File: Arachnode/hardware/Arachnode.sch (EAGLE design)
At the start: 35 parts, among them J1 PINHEAD-17-REV, J2 PINHEAD-17-REV, U1 BQ24210, U2 DS1337

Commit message: ﻿-- added power switching to make USB power work correctly. # Please enter the commit message for your changes. Lines starting # with '#' will be ignored, and an empty message aborts the commit. # On branch arachnode-update # Your branch is up-to-date with 'origin/arachnode-update'. # # Changes to be committed: #	modified:   Arachnode/hardware/Arachnode.brd #	modified:   Arachnode/hardware/Arachnode.sch #
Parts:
- added R15: 4k7, resistor:R-EU_R0603
- added T1: (no value), zetex:PMOSSOT23
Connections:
- new net 3V3: J2.16, J2.33, JP2.16, T1.D
- net +5V: now also R15.2
- net N$1: now also R15.1, T1.G; no longer C1.2, R1.2, SOLAR.1A, SOLAR.1B, U1.VIN
- net VIN: now also C1.2, R1.2, SOLAR.1A, SOLAR.1B, U1.VIN
- net V_BATT: now also T1.S; no longer J2.16, J2.33, JP2.16
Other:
- moved on the sheet: SD
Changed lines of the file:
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@@
 <part name="C4" library="resistor" deviceset="C-EU" device="C0603" value="100n"/>
 <part name="GND14" library="supply1" deviceset="GND" device=""/>
+<part name="T1" library="zetex" deviceset="PMOSSOT23" device=""/>
+<part name="R15" library="resistor" deviceset="R-EU_" device="R0603" value="4k7"/>
 </parts>
 <sheets>
@@
 <instance part="GND1" gate="1" x="48.26" y="114.3"/>
 <instance part="GND2" gate="1" x="167.64" y="114.3"/>
-<instance part="SD" gate="G$1" x="231.14" y="144.78">
-<attribute name="PARTNO" x="231.14" y="144.78" size="1.778" layer="96" display="off"/>
-</instance>
-<instance part="GND3" gate="1" x="218.44" y="116.84"/>
-<instance part="SUPPLY4" gate="G$1" x="170.18" y="172.72"/>
-<instance part="SUPPLY6" gate="G$1" x="220.98" y="165.1"/>
+<instance part="SD" gate="G$1" x="53.34" y="68.58">
+<attribute name="PARTNO" x="53.34" y="68.58" size="1.778" layer="96" display="off"/>
+</instance>
+<instance part="GND3" gate="1" x="40.64" y="40.64"/>
+<instance part="SUPPLY4" gate="G$1" x="228.6" y="129.54"/>
+<instance part="SUPPLY6" gate="G$1" x="43.18" y="88.9"/>
 <instance part="J1" gate="G$1" x="68.58" y="142.24"/>
 <instance part="J2" gate="G$1" x="160.02" y="142.24" rot="MR0"/>
@@
 <instance part="C4" gate="G$1" x="93.98" y="104.14"/>
 <instance part="GND14" gate="1" x="93.98" y="93.98"/>
+<instance part="T1" gate="A" x="218.44" y="124.46" rot="MR270"/>
+<instance part="R15" gate="G$1" x="203.2" y="149.86" rot="R180"/>
 </instances>
 <busses>
@@
 <segment>
 <pinref part="SD" gate="G$1" pin="CS"/>
-<wire x1="223.52" y1="154.94" x2="208.28" y2="154.94" width="0.1524" layer="91"/>
-<label x="208.28" y="154.94" size="1.778" layer="95"/>
+<wire x1="45.72" y1="78.74" x2="30.48" y2="78.74" width="0.1524" layer="91"/>
+<label x="30.48" y="78.74" size="1.778" layer="95"/>
 </segment>
 </net>
@@
 <segment>
 <pinref part="SD" gate="G$1" pin="GND"/>
-<wire x1="223.52" y1="144.78" x2="218.44" y2="144.78" width="0.1524" layer="91"/>
-<wire x1="218.44" y1="144.78" x2="218.44" y2="134.62" width="0.1524" layer="91"/>
+<wire x1="45.72" y1="68.58" x2="40.64" y2="68.58" width="0.1524" layer="91"/>
+<wire x1="40.64" y1="68.58" x2="40.64" y2="58.42" width="0.1524" layer="91"/>
 <pinref part="SD" gate="G$1" pin="SHIELD@1"/>
-<wire x1="218.44" y1="134.62" x2="218.44" y2="132.08" width="0.1524" layer="91"/>
-<wire x1="218.44" y1="132.08" x2="218.44" y2="129.54" width="0.1524" layer="91"/>
-<wire x1="218.44" y1="129.54" x2="218.44" y2="127" width="0.1524" layer="91"/>
-<wire x1="218.44" y1="127" x2="218.44" y2="119.38" width="0.1524" layer="91"/>
-<wire x1="223.52" y1="134.62" x2="218.44" y2="134.62" width="0.1524" layer="91"/>
+<wire x1="40.64" y1="58.42" x2="40.64" y2="55.88" width="0.1524" layer="91"/>
+<wire x1="40.64" y1="55.88" x2="40.64" y2="53.34" width="0.1524" layer="91"/>
+<wire x1="40.64" y1="53.34" x2="40.64" y2="50.8" width="0.1524" layer="91"/>
+<wire x1="40.64" y1="50.8" x2="40.64" y2="43.18" width="0.1524" layer="91"/>
+<wire x1="45.72" y1="58.42" x2="40.64" y2="58.42" width="0.1524" layer="91"/>
 <pinref part="SD" gate="G$1" pin="SHIELD@2"/>
-<wire x1="223.52" y1="132.08" x2="218.44" y2="132.08" width="0.1524" layer="91"/>
+<wire x1="45.72" y1="55.88" x2="40.64" y2="55.88" width="0.1524" layer="91"/>
 <pinref part="SD" gate="G$1" pin="SHIELD@3"/>
-<wire x1="223.52" y1="129.54" x2="218.44" y2="129.54" width="0.1524" layer="91"/>
+<wire x1="45.72" y1="53.34" x2="40.64" y2="53.34" width="0.1524" layer="91"/>
 <pinref part="SD" gate="G$1" pin="SHIELD@4"/>
-<wire x1="223.52" y1="127" x2="218.44" y2="127" width="0.1524" layer="91"/>
+<wire x1="45.72" y1="50.8" x2="40.64" y2="50.8" width="0.1524" layer="91"/>
 <pinref part="GND3" gate="1" pin="GND"/>
-<junction x="218.44" y="127"/>
-<junction x="218.44" y="129.54"/>
-<junction x="218.44" y="132.08"/>
-<junction x="218.44" y="134.62"/>
+<junction x="40.64" y="50.8"/>
+<junction x="40.64" y="53.34"/>
+<junction x="40.64" y="55.88"/>
+<junction x="40.64" y="58.42"/>
 </segment>
 <segment>
@@
 <segment>
 <pinref part="SD" gate="G$1" pin="DO"/>
-<wire x1="223.52" y1="142.24" x2="208.28" y2="142.24" width="0.1524" layer="91"/>
-<label x="208.28" y="142.24" size="1.778" layer="95"/>
+<wire x1="45.72" y1="66.04" x2="30.48" y2="66.04" width="0.1524" layer="91"/>
+<label x="30.48" y="66.04" size="1.778" layer="95"/>
 </segment>
 </net>
@@
 <segment>
 <pinref part="SD" gate="G$1" pin="SCK"/>
-<wire x1="223.52" y1="147.32" x2="208.28" y2="147.32" width="0.1524" layer="91"/>
-<label x="208.28" y="147.32" size="1.778" layer="95"/>
+<wire x1="45.72" y1="71.12" x2="30.48" y2="71.12" width="0.1524" layer="91"/>
+<label x="30.48" y="71.12" size="1.778" layer="95"/>
 </segment>
 </net>
@@
 <segment>
 <pinref part="SD" gate="G$1" pin="DI"/>
-<wire x1="223.52" y1="152.4" x2="208.28" y2="152.4" width="0.1524" layer="91"/>
-<label x="208.28" y="152.4" size="1.778" layer="95"/>
+<wire x1="45.72" y1="76.2" x2="30.48" y2="76.2" width="0.1524" layer="91"/>
+<label x="30.48" y="76.2" size="1.778" layer="95"/>
 </segment>
 </net>
@@
 <junction x="162.56" y="149.86"/>
 <pinref part="JP2" gate="G$1" pin="6"/>
+<pinref part="R15" gate="G$1" pin="2"/>
+<wire x1="190.5" y1="149.86" x2="198.12" y2="149.86" width="0.1524" layer="91"/>
+<junction x="190.5" y="149.86"/>
 </segment>
 </net>
 <net name="V_BATT" class="0">
 <segment>
-<wire x1="190.5" y1="124.46" x2="170.18" y2="124.46" width="0.1524" layer="91"/>
-<label x="172.72" y="124.46" size="1.778" layer="95"/>
-<wire x1="170.18" y1="124.46" x2="162.56" y2="124.46" width="0.1524" layer="91"/>
-<wire x1="170.18" y1="124.46" x2="170.18" y2="172.72" width="0.1524" layer="91"/>
-<junction x="170.18" y="124.46"/>
-<pinref part="SUPPLY4" gate="G$1" pin="V_BATT"/>
-<pinref part="J2" gate="G$1" pin="16"/>
-<pinref part="J2" gate="G$1" pin="33"/>
-<junction x="162.56" y="124.46"/>
-<pinref part="JP2" gate="G$1" pin="16"/>
-</segment>
-<segment>
 <pinref part="SD" gate="G$1" pin="VCC"/>
-<wire x1="223.52" y1="149.86" x2="220.98" y2="149.86" width="0.1524" layer="91"/>
-<wire x1="220.98" y1="149.86" x2="220.98" y2="165.1" width="0.1524" layer="91"/>
+<wire x1="45.72" y1="73.66" x2="43.18" y2="73.66" width="0.1524" layer="91"/>
+<wire x1="43.18" y1="73.66" x2="43.18" y2="88.9" width="0.1524" layer="91"/>
 <pinref part="SUPPLY6" gate="G$1" pin="V_BATT"/>
 </segment>
@@
 <junction x="93.98" y="111.76"/>
 </segment>
+<segment>
+<pinref part="T1" gate="A" pin="S"/>
+<pinref part="SUPPLY4" gate="G$1" pin="V_BATT"/>
+<wire x1="223.52" y1="124.46" x2="228.6" y2="124.46" width="0.1524" layer="91"/>
+<wire x1="228.6" y1="124.46" x2="228.6" y2="129.54" width="0.1524" layer="91"/>
+</segment>
 </net>
 <net name="IO12" class="0">
@@
 <wire x1="88.9" y1="129.54" x2="139.7" y2="129.54" width="0.1524" layer="91"/>
 <wire x1="139.7" y1="129.54" x2="139.7" y2="147.32" width="0.1524" layer="91"/>
+</segment>
+</net>
+<net name="N$1" class="0">
+<segment>
+<pinref part="R15" gate="G$1" pin="1"/>
+<pinref part="T1" gate="A" pin="G"/>
+<wire x1="208.28" y1="149.86" x2="220.98" y2="149.86" width="0.1524" layer="91"/>
+<wire x1="220.98" y1="149.86" x2="220.98" y2="129.54" width="0.1524" layer="91"/>
+</segment>
+</net>
+<net name="3V3" class="0">
+<segment>
+<wire x1="190.5" y1="124.46" x2="162.56" y2="124.46" width="0.1524" layer="91"/>
+<label x="172.72" y="124.46" size="1.778" layer="95"/>
+<pinref part="J2" gate="G$1" pin="16"/>
+<pinref part="J2" gate="G$1" pin="33"/>
+<junction x="162.56" y="124.46"/>
+<pinref part="JP2" gate="G$1" pin="16"/>
+<junction x="190.5" y="124.46"/>
+<pinref part="T1" gate="A" pin="D"/>
+<wire x1="190.5" y1="124.46" x2="213.36" y2="124.46" width="0.1524" layer="91"/>
 </segment>
 </net>
@@
 </segment>
 </net>
-<net name="N$1" class="0">
+<net name="VIN" class="0">
 <segment>
 <wire x1="38.1" y1="124.46" x2="48.26" y2="124.46" width="0.1524" layer="91"/>
@@
 <wire x1="71.12" y1="114.3" x2="71.12" y2="124.46" width="0.1524" layer="91"/>
 <junction x="71.12" y="124.46"/>
-</segment>
-</net>
+<label x="58.42" y="124.46" size="1.778" layer="95"/>
+</segment>
+</net>

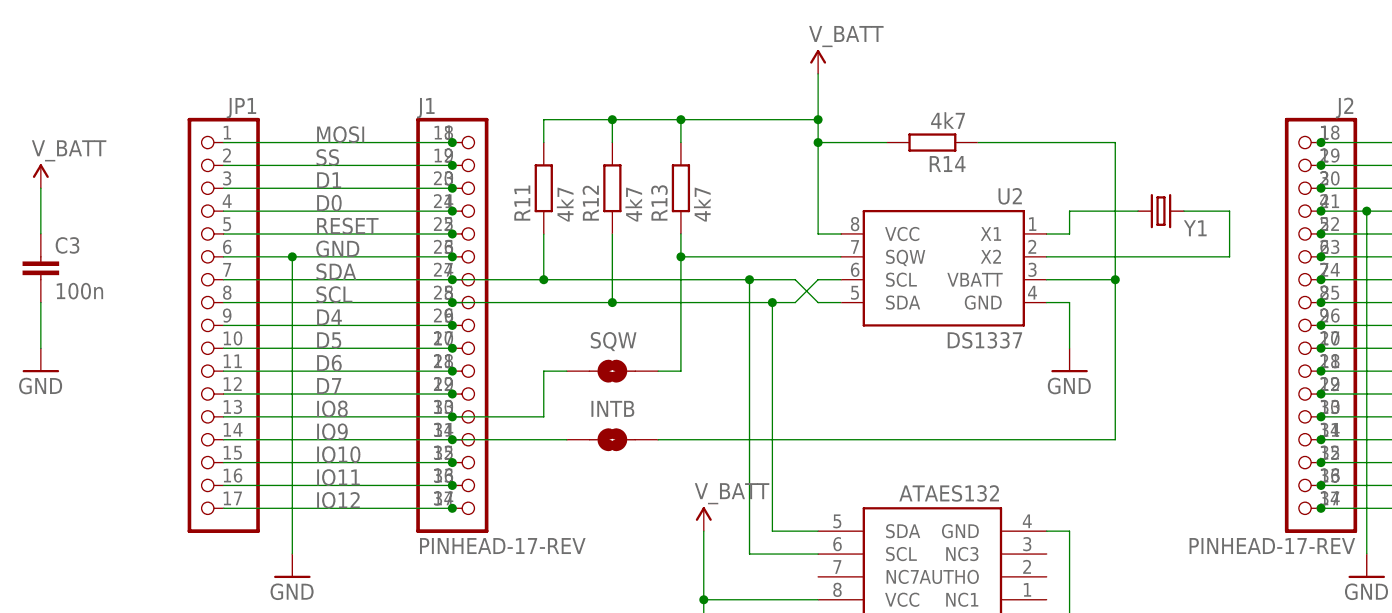
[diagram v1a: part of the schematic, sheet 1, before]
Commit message: Modified ArachnNode to Arachnio Due standard
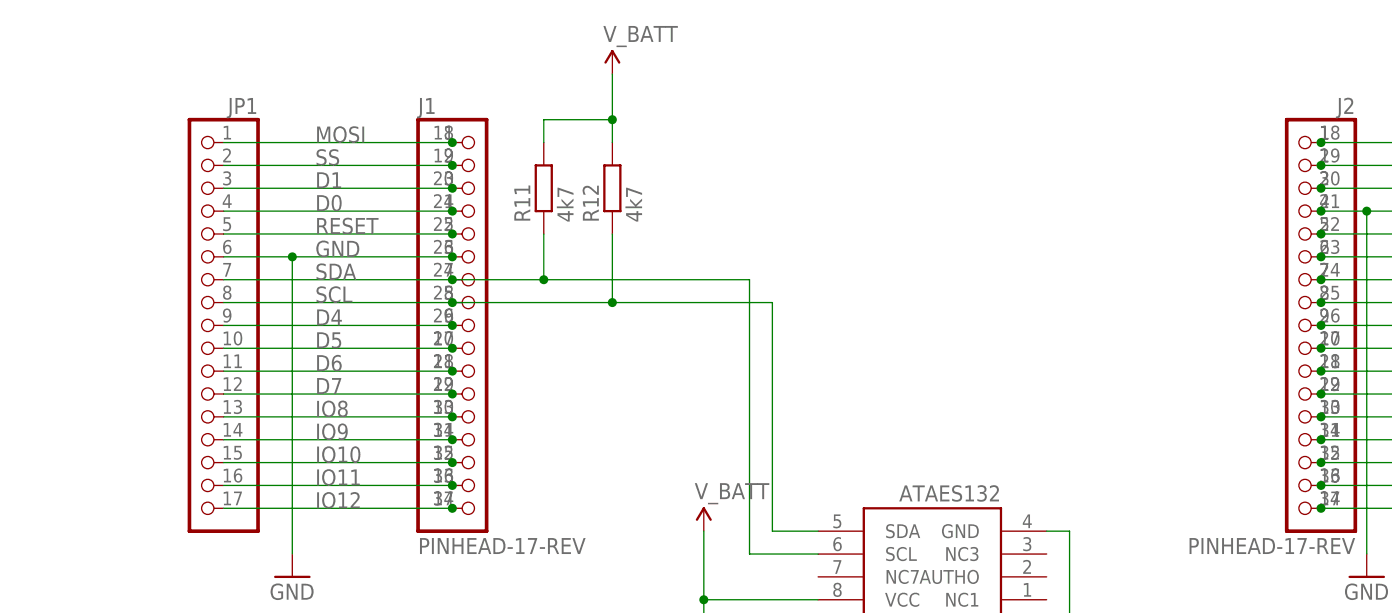
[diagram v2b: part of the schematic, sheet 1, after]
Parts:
- removed C3: 100n, resistor:C-EUC0603
- removed INTB, SQW: JUMPER-PAD-2-NOYES_SILK, SparkFun-Passives:JUMPER-PAD-2-NOYES_SILK
- removed R13, R14: 4k7, resistor:R-EU_R0603
- removed U2: DS1337, SparkFun-FreqCtrl:DS1307SO8-TIGHT
- removed Y1: (no value), SparkFun-FreqCtrl:CRYSTALEPSONMC146
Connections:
- removed net N$14: U2.X2, Y1.2
- removed net N$15: INTB.2, R14.1, U2.VBATT
- removed net N$2: R13.1, SQW.2, U2.SQW
- removed net N$4: U2.X1, Y1.1
- net GND: no longer C3.2, U2.GND
- net IO8: no longer SQW.1
- net IO9: no longer INTB.1
- net SCL: no longer U2.SCL
- net SDA: no longer U2.SDA
- net V_BATT: no longer C3.1, R13.2, R14.2, U2.VCC
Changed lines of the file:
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@@
 <part name="!CHG!" library="SparkFun-Passives" deviceset="JUMPER-PAD-2-NC_BY_TRACE" device=""/>
 <part name="!PG!" library="SparkFun-Passives" deviceset="JUMPER-PAD-2-NC_BY_TRACE" device=""/>
-<part name="U2" library="SparkFun-FreqCtrl" deviceset="DS1307" device="SO8-TIGHT" value="DS1337"/>
 <part name="SUPPLY2" library="SparkFun-Aesthetics" deviceset="V_BATT" device=""/>
-<part name="GND11" library="supply1" deviceset="GND" device=""/>
-<part name="C3" library="resistor" deviceset="C-EU" device="C0603" value="100n"/>
 <part name="R11" library="resistor" deviceset="R-EU_" device="R0603" value="4k7"/>
 <part name="R12" library="resistor" deviceset="R-EU_" device="R0603" value="4k7"/>
-<part name="SQW" library="SparkFun-Passives" deviceset="JUMPER-PAD-2-NO" device="YES_SILK" value=""/>
-<part name="SUPPLY3" library="SparkFun-Aesthetics" deviceset="V_BATT" device=""/>
-<part name="GND12" library="supply1" deviceset="GND" device=""/>
-<part name="Y1" library="SparkFun-FreqCtrl" deviceset="CRYSTAL" device="EPSONMC146"/>
-<part name="R13" library="resistor" deviceset="R-EU_" device="R0603" value="4k7"/>
-<part name="R14" library="resistor" deviceset="R-EU_" device="R0603" value="4k7"/>
-<part name="INTB" library="SparkFun-Passives" deviceset="JUMPER-PAD-2-NO" device="YES_SILK" value=""/>
 <part name="AES1" library="SparkFun-DigitalIC" deviceset="ATAES132" device=""/>
 <part name="GND13" library="supply1" deviceset="GND" device=""/>
@@
 <instance part="JP1" gate="G$1" x="38.1" y="144.78" rot="MR0"/>
 <instance part="JP2" gate="G$1" x="193.04" y="144.78"/>
-<instance part="U2" gate="G$1" x="121.92" y="149.86" rot="MR0"/>
-<instance part="SUPPLY2" gate="G$1" x="106.68" y="170.18"/>
-<instance part="GND11" gate="1" x="134.62" y="137.16"/>
-<instance part="C3" gate="G$1" x="20.32" y="149.86"/>
+<instance part="SUPPLY2" gate="G$1" x="83.82" y="170.18"/>
 <instance part="R11" gate="G$1" x="76.2" y="157.48" rot="R90"/>
 <instance part="R12" gate="G$1" x="83.82" y="157.48" rot="R90"/>
-<instance part="SQW" gate="G$1" x="83.82" y="137.16"/>
-<instance part="SUPPLY3" gate="G$1" x="20.32" y="157.48"/>
-<instance part="GND12" gate="1" x="20.32" y="137.16"/>
-<instance part="Y1" gate="G$1" x="144.78" y="154.94" rot="MR180"/>
-<instance part="R13" gate="G$1" x="91.44" y="157.48" rot="R90"/>
-<instance part="R14" gate="G$1" x="119.38" y="162.56" rot="R180"/>
-<instance part="INTB" gate="G$1" x="83.82" y="129.54"/>
 <instance part="AES1" gate="G$1" x="119.38" y="114.3" rot="R180"/>
 <instance part="GND13" gate="1" x="134.62" y="104.14"/>
@@
 <wire x1="66.04" y1="147.32" x2="76.2" y2="147.32" width="0.1524" layer="91"/>
 <wire x1="76.2" y1="147.32" x2="99.06" y2="147.32" width="0.1524" layer="91"/>
-<wire x1="99.06" y1="147.32" x2="104.14" y2="147.32" width="0.1524" layer="91"/>
-<wire x1="104.14" y1="147.32" x2="106.68" y2="144.78" width="0.1524" layer="91"/>
-<pinref part="U2" gate="G$1" pin="SDA"/>
-<wire x1="106.68" y1="144.78" x2="109.22" y2="144.78" width="0.1524" layer="91"/>
 <pinref part="R11" gate="G$1" pin="1"/>
 <wire x1="76.2" y1="152.4" x2="76.2" y2="147.32" width="0.1524" layer="91"/>
@@
 <wire x1="106.68" y1="116.84" x2="99.06" y2="116.84" width="0.1524" layer="91"/>
 <wire x1="99.06" y1="116.84" x2="99.06" y2="147.32" width="0.1524" layer="91"/>
-<junction x="99.06" y="147.32"/>
 </segment>
 </net>
@@
 <wire x1="66.04" y1="144.78" x2="83.82" y2="144.78" width="0.1524" layer="91"/>
 <wire x1="83.82" y1="144.78" x2="101.6" y2="144.78" width="0.1524" layer="91"/>
-<wire x1="101.6" y1="144.78" x2="104.14" y2="144.78" width="0.1524" layer="91"/>
-<wire x1="104.14" y1="144.78" x2="106.68" y2="147.32" width="0.1524" layer="91"/>
-<pinref part="U2" gate="G$1" pin="SCL"/>
-<wire x1="106.68" y1="147.32" x2="109.22" y2="147.32" width="0.1524" layer="91"/>
 <pinref part="R12" gate="G$1" pin="1"/>
 <wire x1="83.82" y1="152.4" x2="83.82" y2="144.78" width="0.1524" layer="91"/>
@@
 <wire x1="106.68" y1="119.38" x2="101.6" y2="119.38" width="0.1524" layer="91"/>
 <wire x1="101.6" y1="119.38" x2="101.6" y2="144.78" width="0.1524" layer="91"/>
-<junction x="101.6" y="144.78"/>
 </segment>
 </net>
@@
 <junction x="66.04" y="129.54"/>
 <pinref part="JP1" gate="G$1" pin="14"/>
-<pinref part="INTB" gate="G$1" pin="1"/>
-<wire x1="78.74" y1="129.54" x2="66.04" y2="129.54" width="0.1524" layer="91"/>
 </segment>
 </net>
@@
 </segment>
 <segment>
-<pinref part="U2" gate="G$1" pin="GND"/>
-<pinref part="GND11" gate="1" pin="GND"/>
-<wire x1="132.08" y1="144.78" x2="134.62" y2="144.78" width="0.1524" layer="91"/>
-<wire x1="134.62" y1="144.78" x2="134.62" y2="139.7" width="0.1524" layer="91"/>
-</segment>
-<segment>
-<pinref part="C3" gate="G$1" pin="2"/>
-<pinref part="GND12" gate="1" pin="GND"/>
-<wire x1="20.32" y1="139.7" x2="20.32" y2="144.78" width="0.1524" layer="91"/>
-</segment>
-<segment>
 <pinref part="AES1" gate="G$1" pin="GND"/>
 <pinref part="GND13" gate="1" pin="GND"/>
@@
 <junction x="66.04" y="132.08"/>
 <pinref part="JP1" gate="G$1" pin="13"/>
-<wire x1="66.04" y1="132.08" x2="76.2" y2="132.08" width="0.1524" layer="91"/>
-<wire x1="76.2" y1="132.08" x2="76.2" y2="137.16" width="0.1524" layer="91"/>
-<pinref part="SQW" gate="G$1" pin="1"/>
-<wire x1="76.2" y1="137.16" x2="78.74" y2="137.16" width="0.1524" layer="91"/>
 </segment>
 </net>
@@
 </segment>
 <segment>
-<pinref part="U2" gate="G$1" pin="VCC"/>
-<wire x1="109.22" y1="152.4" x2="106.68" y2="152.4" width="0.1524" layer="91"/>
 <pinref part="SUPPLY2" gate="G$1" pin="V_BATT"/>
-<wire x1="106.68" y1="152.4" x2="106.68" y2="162.56" width="0.1524" layer="91"/>
 <pinref part="R12" gate="G$1" pin="2"/>
-<wire x1="106.68" y1="162.56" x2="106.68" y2="165.1" width="0.1524" layer="91"/>
-<wire x1="106.68" y1="165.1" x2="106.68" y2="170.18" width="0.1524" layer="91"/>
-<wire x1="106.68" y1="165.1" x2="91.44" y2="165.1" width="0.1524" layer="91"/>
-<wire x1="91.44" y1="165.1" x2="83.82" y2="165.1" width="0.1524" layer="91"/>
+<wire x1="83.82" y1="170.18" x2="83.82" y2="165.1" width="0.1524" layer="91"/>
 <wire x1="83.82" y1="165.1" x2="83.82" y2="162.56" width="0.1524" layer="91"/>
 <pinref part="R11" gate="G$1" pin="2"/>
@@
 <wire x1="76.2" y1="165.1" x2="76.2" y2="162.56" width="0.1524" layer="91"/>
 <junction x="83.82" y="165.1"/>
-<junction x="106.68" y="165.1"/>
-<pinref part="R13" gate="G$1" pin="2"/>
-<wire x1="91.44" y1="162.56" x2="91.44" y2="165.1" width="0.1524" layer="91"/>
-<junction x="91.44" y="165.1"/>
-<pinref part="R14" gate="G$1" pin="2"/>
-<wire x1="114.3" y1="162.56" x2="106.68" y2="162.56" width="0.1524" layer="91"/>
-<junction x="106.68" y="162.56"/>
-</segment>
-<segment>
-<pinref part="C3" gate="G$1" pin="1"/>
-<pinref part="SUPPLY3" gate="G$1" pin="V_BATT"/>
-<wire x1="20.32" y1="157.48" x2="20.32" y2="152.4" width="0.1524" layer="91"/>
 </segment>
 <segment>
@@
 </segment>
 </net>
-<net name="N$2" class="0">
-<segment>
-<pinref part="U2" gate="G$1" pin="SQW"/>
-<wire x1="109.22" y1="149.86" x2="91.44" y2="149.86" width="0.1524" layer="91"/>
-<wire x1="91.44" y1="149.86" x2="91.44" y2="137.16" width="0.1524" layer="91"/>
-<pinref part="SQW" gate="G$1" pin="2"/>
-<wire x1="91.44" y1="137.16" x2="88.9" y2="137.16" width="0.1524" layer="91"/>
-<pinref part="R13" gate="G$1" pin="1"/>
-<wire x1="91.44" y1="152.4" x2="91.44" y2="149.86" width="0.1524" layer="91"/>
-<junction x="91.44" y="149.86"/>
-</segment>
-</net>
-<net name="N$4" class="0">
-<segment>
-<wire x1="134.62" y1="154.94" x2="134.62" y2="152.4" width="0.1524" layer="91"/>
-<pinref part="U2" gate="G$1" pin="X1"/>
-<wire x1="134.62" y1="152.4" x2="132.08" y2="152.4" width="0.1524" layer="91"/>
-<pinref part="Y1" gate="G$1" pin="1"/>
-<wire x1="142.24" y1="154.94" x2="134.62" y2="154.94" width="0.1524" layer="91"/>
-</segment>
-</net>
-<net name="N$14" class="0">
-<segment>
-<pinref part="U2" gate="G$1" pin="X2"/>
-<wire x1="132.08" y1="149.86" x2="152.4" y2="149.86" width="0.1524" layer="91"/>
-<wire x1="152.4" y1="149.86" x2="152.4" y2="154.94" width="0.1524" layer="91"/>
-<pinref part="Y1" gate="G$1" pin="2"/>
-<wire x1="147.32" y1="154.94" x2="152.4" y2="154.94" width="0.1524" layer="91"/>
-</segment>
-</net>
-<net name="N$15" class="0">
-<segment>
-<pinref part="R14" gate="G$1" pin="1"/>
-<wire x1="124.46" y1="162.56" x2="139.7" y2="162.56" width="0.1524" layer="91"/>
-<wire x1="139.7" y1="162.56" x2="139.7" y2="147.32" width="0.1524" layer="91"/>
-<pinref part="U2" gate="G$1" pin="VBATT"/>
-<wire x1="139.7" y1="147.32" x2="132.08" y2="147.32" width="0.1524" layer="91"/>
-<junction x="139.7" y="147.32"/>
-<pinref part="INTB" gate="G$1" pin="2"/>
-<wire x1="88.9" y1="129.54" x2="139.7" y2="129.54" width="0.1524" layer="91"/>
-<wire x1="139.7" y1="129.54" x2="139.7" y2="147.32" width="0.1524" layer="91"/>
-</segment>
-</net>

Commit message: Fixed the Arachnode so it's got triple row headers on the passthroughs
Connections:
- net +5V: now also J2.40
- net 3V3: now also J2.50
- net A0: now also J2.48
- net A1: now also J2.47
- net A2: now also J2.46
- net A3: now also J2.45
- net A4: now also J2.44
- net A5: now also J2.43
- net AREF: now also J2.49
- net D0: now also J1.38
- net D1: now also J1.37
- net D4: now also J1.43
- net D5: now also J1.44
- net D6: now also J1.45
- net D7: now also J1.46
- net ESP_RST: now also J2.42
- net GND: now also J1.40, J2.38
- net IO10: now also J1.49
- net IO11: now also J1.50
- net IO12: now also J1.51
- net IO13: now also J2.51
- net IO8: now also J1.47
- net IO9: now also J1.48
- net MISO: now also J2.36
- net MOSI: now also J1.35
- net RESET: now also J1.39, J2.39
- net SCK: now also J2.35
- net SCL: now also J1.42
- net SDA: now also J1.41
- net SS: now also J1.36
- net TOUT: now also J2.41
- net VIN: now also J2.37
